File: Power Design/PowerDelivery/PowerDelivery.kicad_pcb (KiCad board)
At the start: 2 copper layers, 85 x 85 mm, 29 parts, among them J1 Conn_01x06_Pin, J2 Conn_01x24_Socket, J3 Screw_Terminal_01x08, Q1 Q_NPN_CBE, U1 Opamp_Dual, U2 Opamp_Dual, U3 2EDN8524FXTMA1, U4 IPP016N06NF2SAKMA1, U5 Opamp_Dual

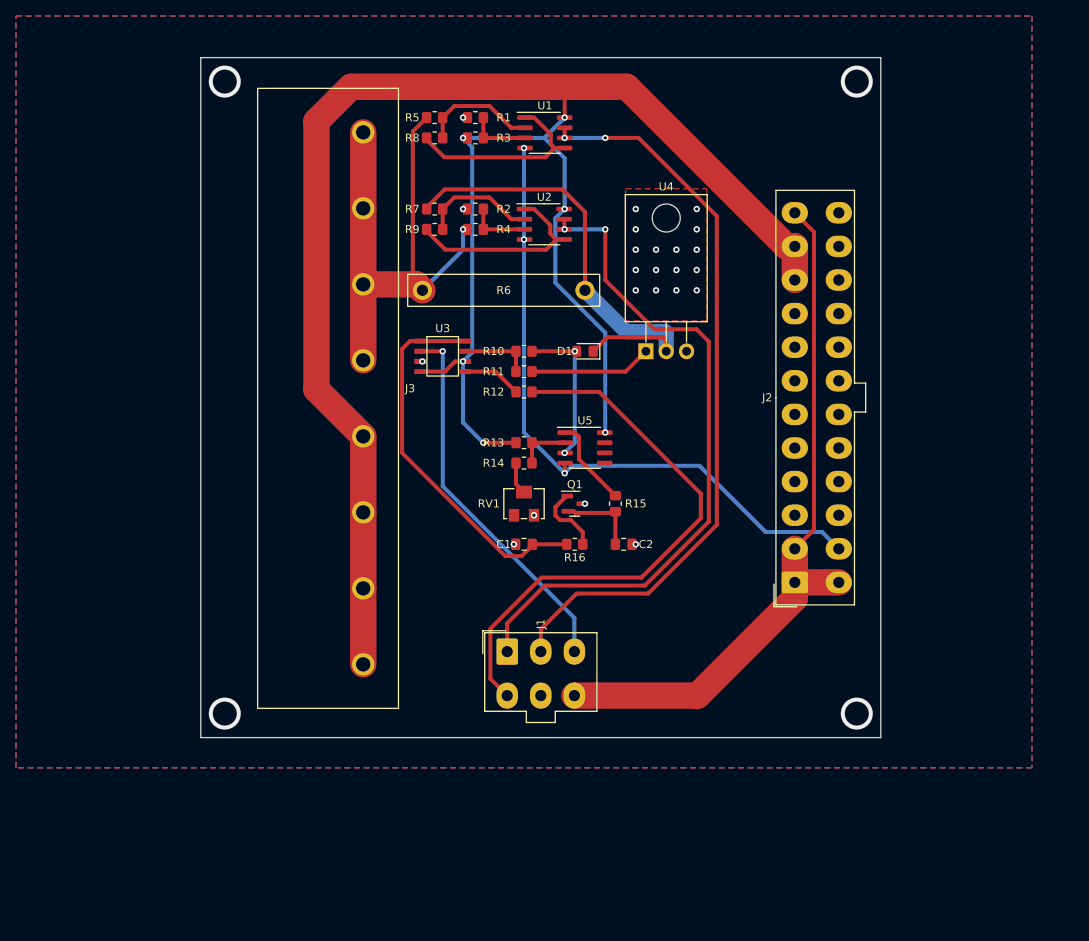
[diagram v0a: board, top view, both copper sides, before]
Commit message: thickened traces
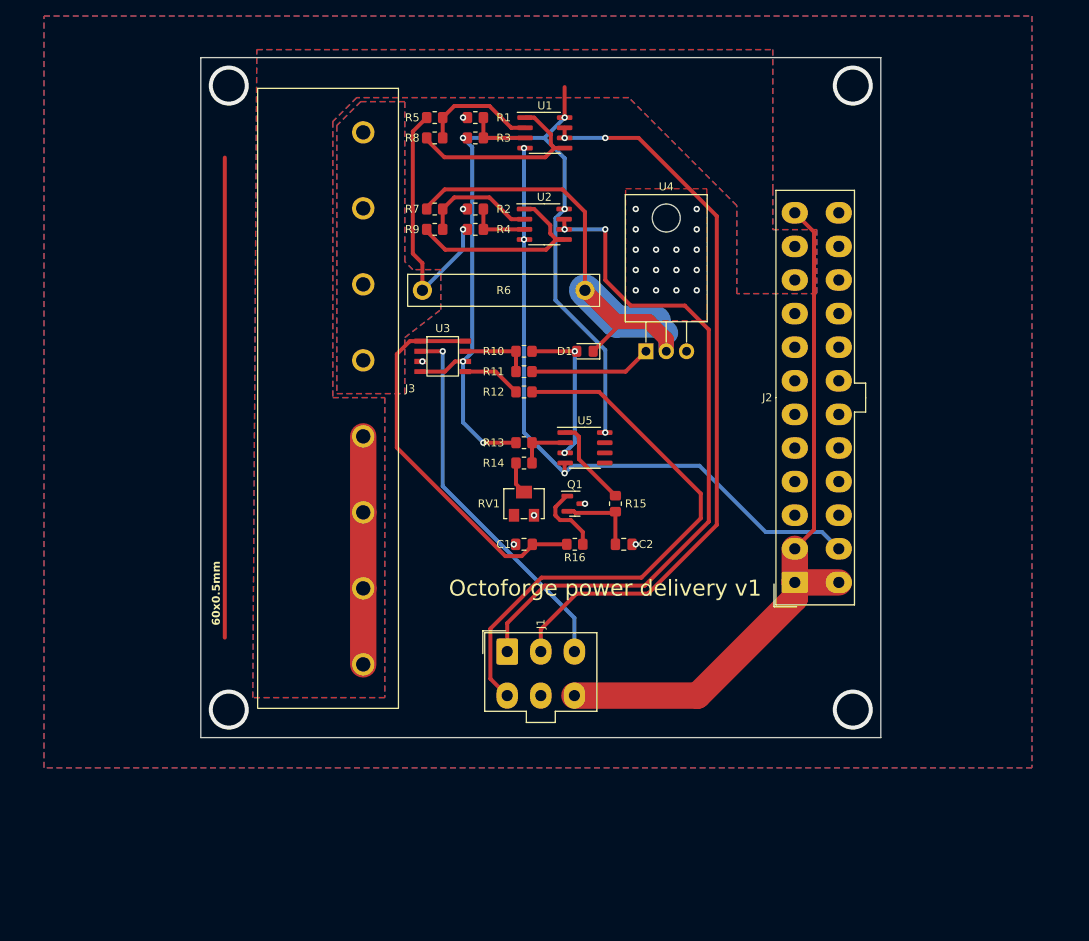
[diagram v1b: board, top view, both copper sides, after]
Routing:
- net +12V: track 253.2 -> 137.4 mm
- net (no net): track 0.00 -> 60.0 mm
- net load: track 68.7 -> 32.5 mm
- net Net-(D1-K): track 59.7 -> 66.0 mm
- net current_sense_out: track 85.4 -> 86.3 mm
- net Net-(U3-ENA): track 47.9 -> 48.5 mm
- added copper zone on B.Cu, net +12V
- added copper zone on F.Cu, net +12V
- added copper zone on B.Cu, net load
- added copper zone on F.Cu, net load
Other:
- board text added: "60x0.5mm"
- board text added: "Octoforge power delivery v1"

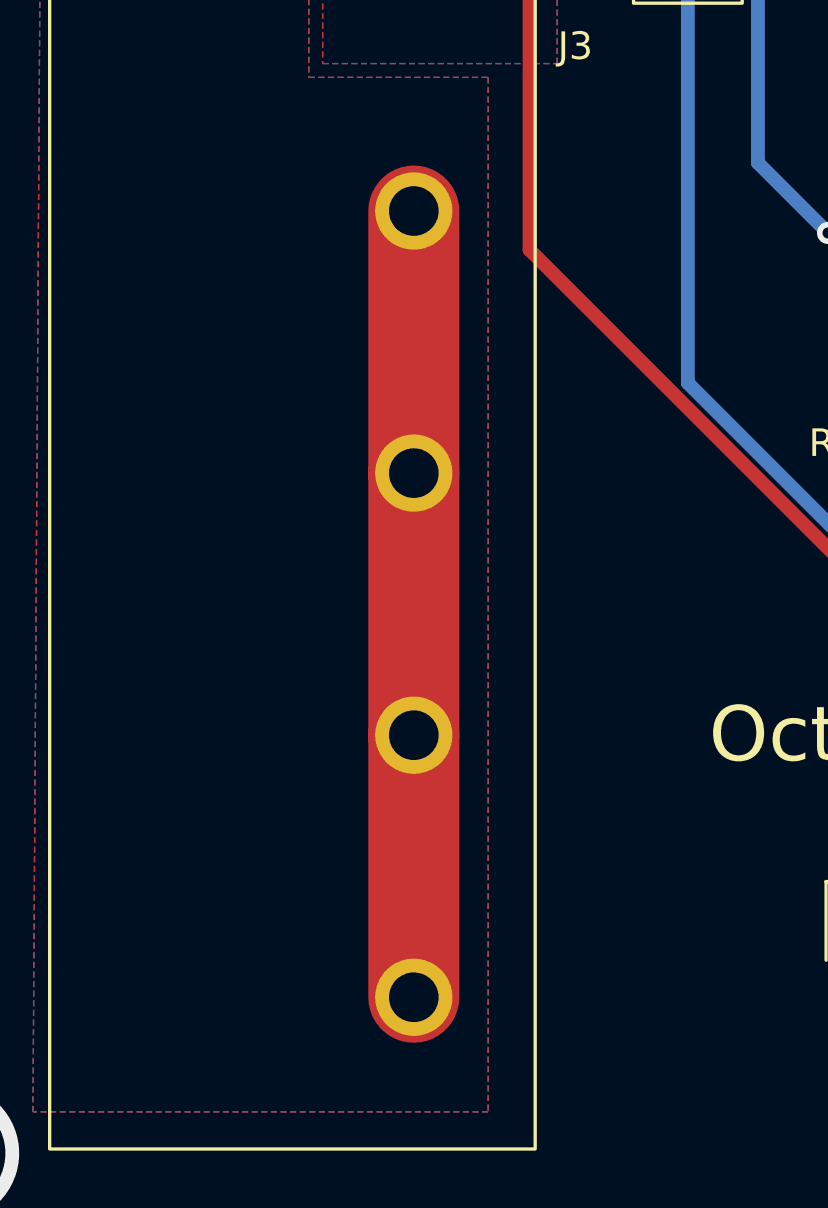
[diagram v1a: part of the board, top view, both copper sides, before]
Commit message: removed uneccessary trace
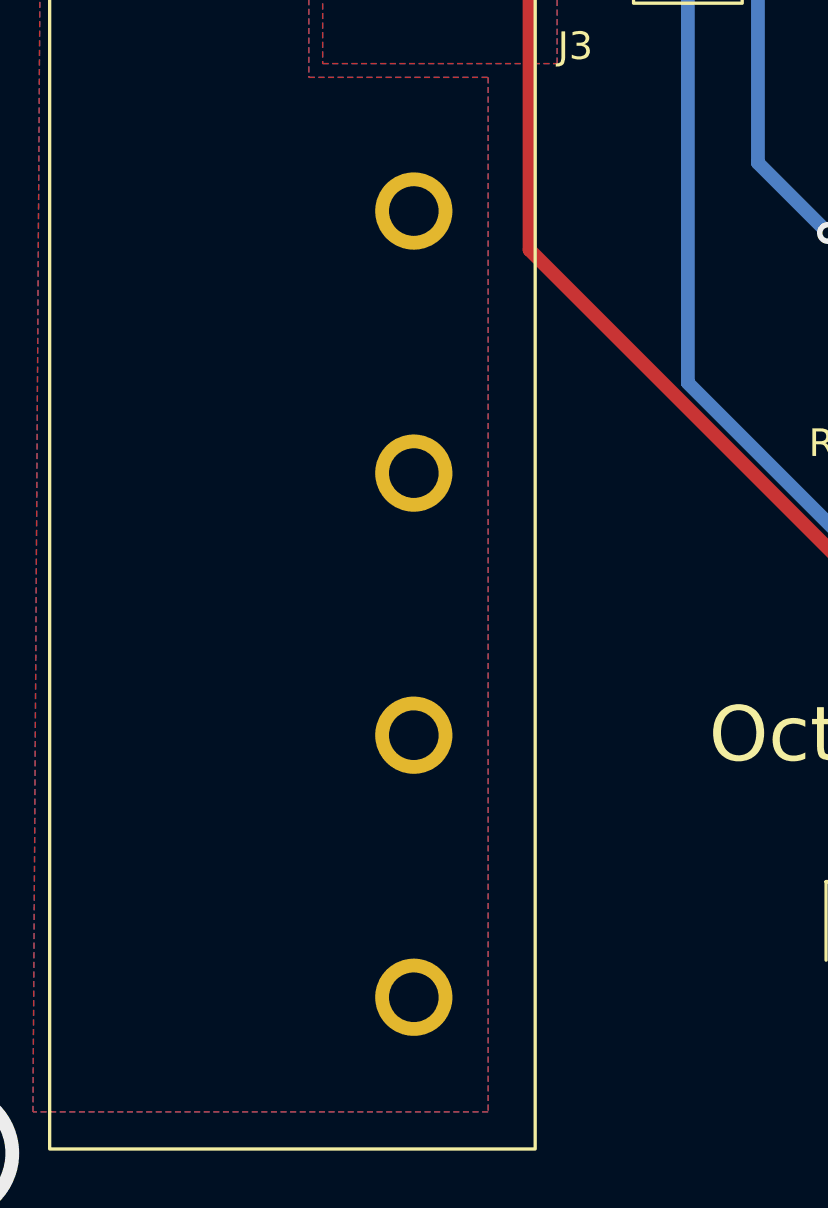
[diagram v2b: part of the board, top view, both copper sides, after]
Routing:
- net +12V: track 137.4 -> 108.9 mm
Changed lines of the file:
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@@
   (segment (start 142.515 95.25) (end 143.785 93.98) (width 0.5) (layer "F.Cu") (net 14))
   (segment (start 147.32 104.14) (end 151.4 104.14) (width 0.5) (layer "F.Cu") (net 14))
-  (segment (start 132.305 122.345) (end 132.305 131.845) (width 3.3) (layer "F.Cu") (net 14))
-  (segment (start 132.305 112.845) (end 132.305 122.345) (width 3.3) (layer "F.Cu") (net 14))
-  (segment (start 132.305 103.345) (end 132.305 112.845) (width 3.3) (layer "F.Cu") (net 14))
   (via (at 157.48 63.5) (size 0.8) (drill 0.4) (layers "F.Cu" "B.Cu") (net 14))
   (via (at 147.32 104.14) (size 0.8) (drill 0.4) (layers "F.Cu" "B.Cu") (free) (net 14))
@@
         (xy 137.5 91)
         (xy 142 87.5)
-        (xy 142 87.5)
         (xy 142 82.5)

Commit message: initial commit
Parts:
- added H1: MountingHole_Pad, MountingHole:MountingHole_3.2mm_M3_ISO7380_Pad, F.Cu at (115.5, 59.5)
- added H2: MountingHole_Pad, MountingHole:MountingHole_3.2mm_M3_ISO7380_Pad, F.Cu at (193.5, 59.5)
- added H3: MountingHole_Pad, MountingHole:MountingHole_3.2mm_M3_ISO7380_Pad, F.Cu at (193.5, 137.5)
- added H4: MountingHole_Pad, MountingHole:MountingHole_3.2mm_M3_ISO7380_Pad, F.Cu at (115.5, 137.5)
- added J4: 8 Pin EPS, Connector_Molex:Molex_Mini-Fit_Jr_5566-08A_2x04_P4.20mm_Vertical, F.Cu at (149.2, 111.2)
- added J5: PS-ON, Connector_PinHeader_2.54mm:PinHeader_1x02_P2.54mm_Vertical, F.Cu at (166.5, 158.0)
- added R17: 1K, Resistor_SMD:R_0805_2012Metric_Pad1.20x1.40mm_HandSolder, F.Cu at (189.1, 71.5)
- added R18: 1K, Resistor_SMD:R_0805_2012Metric_Pad1.20x1.40mm_HandSolder, F.Cu at (190.5, 79.4)
- J1: footprint Connector_Molex:Molex_Mini-Fit_Jr_5566-06A_2x03_P4.20mm_Vertical -> Connector_PinHeader_2.54mm:PinHeader_1x06_P2.54mm_Vertical
- J2: value Conn_01x24_Socket -> 24 Pin ATX
- moved U4 38.6 mm to (144.3, 62.0), turned to -90 degrees
- moved U3 33.0 mm to (175.0, 97.0), turned to -90 degrees
- moved J2 32.7 mm to (156.2, 134.6)
- moved R1 32.0 mm to (175.3, 77.1)
- moved R3 32.0 mm to (175.3, 79.6)
- moved R5 32.0 mm to (170.2, 77.1)
- moved R8 32.0 mm to (170.2, 79.6)
- moved U1 32.0 mm to (184.0, 79.0)
- moved R2 28.2 mm to (173.9, 69.1)
- moved R4 28.2 mm to (173.9, 71.6)
- moved R7 28.2 mm to (168.8, 69.1)
- moved R9 28.2 mm to (168.8, 71.6)
- moved U2 28.2 mm to (182.5, 71.0)
- moved R16 26.6 mm to (182.2, 129.4)
- moved Q1 26.6 mm to (182.2, 124.3)
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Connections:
- J2 pad 16: unconnected-(J2-Pin_16-Pad16) -> Net-(J2-Pin_16)
- U1 pad 6: voltage_sense_out -> unconnected-(U1B---Pad6)
- U1 pad 7: voltage_sense_out -> Net-(R18-Pad1)
- U2 pad 6: current_sense_out -> unconnected-(U2B---Pad6)
- U2 pad 7: current_sense_out -> Net-(R17-Pad1)
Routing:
- net +12V: track 108.9 -> 10.8 mm, vias 6 -> 0
- net voltage_sense_out: track 93.1 -> 0.00 mm, vias 2 -> 0
- net +3.3V: track 88.3 -> 0.00 mm
- net current_sense_out: track 86.3 -> 0.00 mm, vias 2 -> 0
- net -12V: track 83.0 -> 10.8 mm, vias 3 -> 0
- net fault_signal: track 70.7 -> 0.00 mm
- net (no net): track 60.0 -> 0.00 mm
- net Net-(U3-ENA): track 48.5 -> 0.00 mm
- net mc_trigger: track 47.2 -> 0.00 mm, vias 1 -> 0
- net Net-(U2B-+): track 25.0 -> 0.00 mm
- net Net-(U1B-+): track 24.8 -> 0.00 mm
- net Net-(D1-K): track 66.0 -> 42.7 mm
- net Net-(D1-A): track 18.8 -> 0.00 mm, vias 2 -> 0
- net Net-(U4-GATE): track 15.3 -> 0.00 mm
- net Net-(R15-Pad1): track 11.2 -> 0.00 mm
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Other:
- outline, holes or cut-outs redrawn

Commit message: Create power delivery V2
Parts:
- moved J1 68.7 mm to (193.5, 92.2)
- moved J5 33.2 mm to (168.5, 124.8), turned to 180 degrees
- moved C1 22.4 mm to (190.5, 112.5), turned to -90 degrees
- moved RV1 22.3 mm to (169.5, 103.0), turned to 90 degrees
- moved R13 21.5 mm to (173.0, 95.5)
- moved R14 21.5 mm to (173.0, 98.0)
- moved R16 17.7 mm to (187.5, 112.5), turned to 90 degrees
- moved D1 16.1 mm to (178.5, 90.0), turned to -90 degrees
- moved R12 16.0 mm to (188.0, 100.0)
- moved C2 15.5 mm to (178.5, 117.5), turned to 90 degrees
- moved R11 14.8 mm to (181.0, 94.0), turned to -90 degrees
- moved R15 14.8 mm to (178.5, 112.5)
- moved U5 12.0 mm to (173.0, 111.5), turned to -90 degrees
- moved R10 11.6 mm to (178.5, 94.0), turned to -90 degrees
- moved Q1 8.45 mm to (182.9, 115.9), turned to -90 degrees
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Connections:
- C2 pad 1: Net-(Q1-B) -> GND
- C2 pad 2: GND -> Net-(Q1-B)
- J1 pad 1: current_sense_out -> GND
- J1 pad 2: voltage_sense_out -> +3.3V
- J1 pad 5: GND -> current_sense_out
- J1 pad 6: +3.3V -> voltage_sense_out
- J2 pad 12: +3.3V -> unconnected-(J2-Pin_12-Pad12)
- R17 pad 1: Net-(R17-Pad1) -> Net-(U2B--)
- R18 pad 1: Net-(R18-Pad1) -> Net-(U1B--)
- U1 pad 6: unconnected-(U1B---Pad6) -> Net-(U1B--)
- U1 pad 7: Net-(R18-Pad1) -> Net-(U1B--)
- U2 pad 6: unconnected-(U2B---Pad6) -> Net-(U2B--)
- U2 pad 7: Net-(R17-Pad1) -> Net-(U2B--)
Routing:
- net +12V: track 10.8 -> 112.4 mm, vias 0 -> 4
- net +3.3V: track 0.00 -> 67.6 mm
- net -12V: track 10.8 -> 77.6 mm, vias 0 -> 2
- net Net-(U4-GATE): track 0.00 -> 66.1 mm, vias 0 -> 2
- net Net-(D1-K): track 42.7 -> 100.9 mm, vias 0 -> 2
- net current_sense_out: track 0.00 -> 34.0 mm, vias 0 -> 1
- net voltage_sense_out: track 0.00 -> 28.0 mm
- net Net-(U5A--): track 0.00 -> 23.1 mm
- net Net-(U3-ENA): track 0.00 -> 21.6 mm
- net Net-(D1-A): track 0.00 -> 21.0 mm
- net Net-(U1B-+): track 0.00 -> 19.9 mm, vias 0 -> 3
- net Net-(U2B-+): track 0.00 -> 19.8 mm, vias 0 -> 3
- net mc_trigger: track 0.00 -> 19.2 mm, vias 0 -> 1
- net Net-(U3-OUTA): track 0.00 -> 7.92 mm
- net Net-(J2-Pin_16): track 0.00 -> 6.85 mm
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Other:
- board text added: "Octoforge power delivery v2"
- board text removed: "60x0.5mm"
- board text removed: "Octoforge power delivery v1"
